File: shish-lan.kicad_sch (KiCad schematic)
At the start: 4 parts

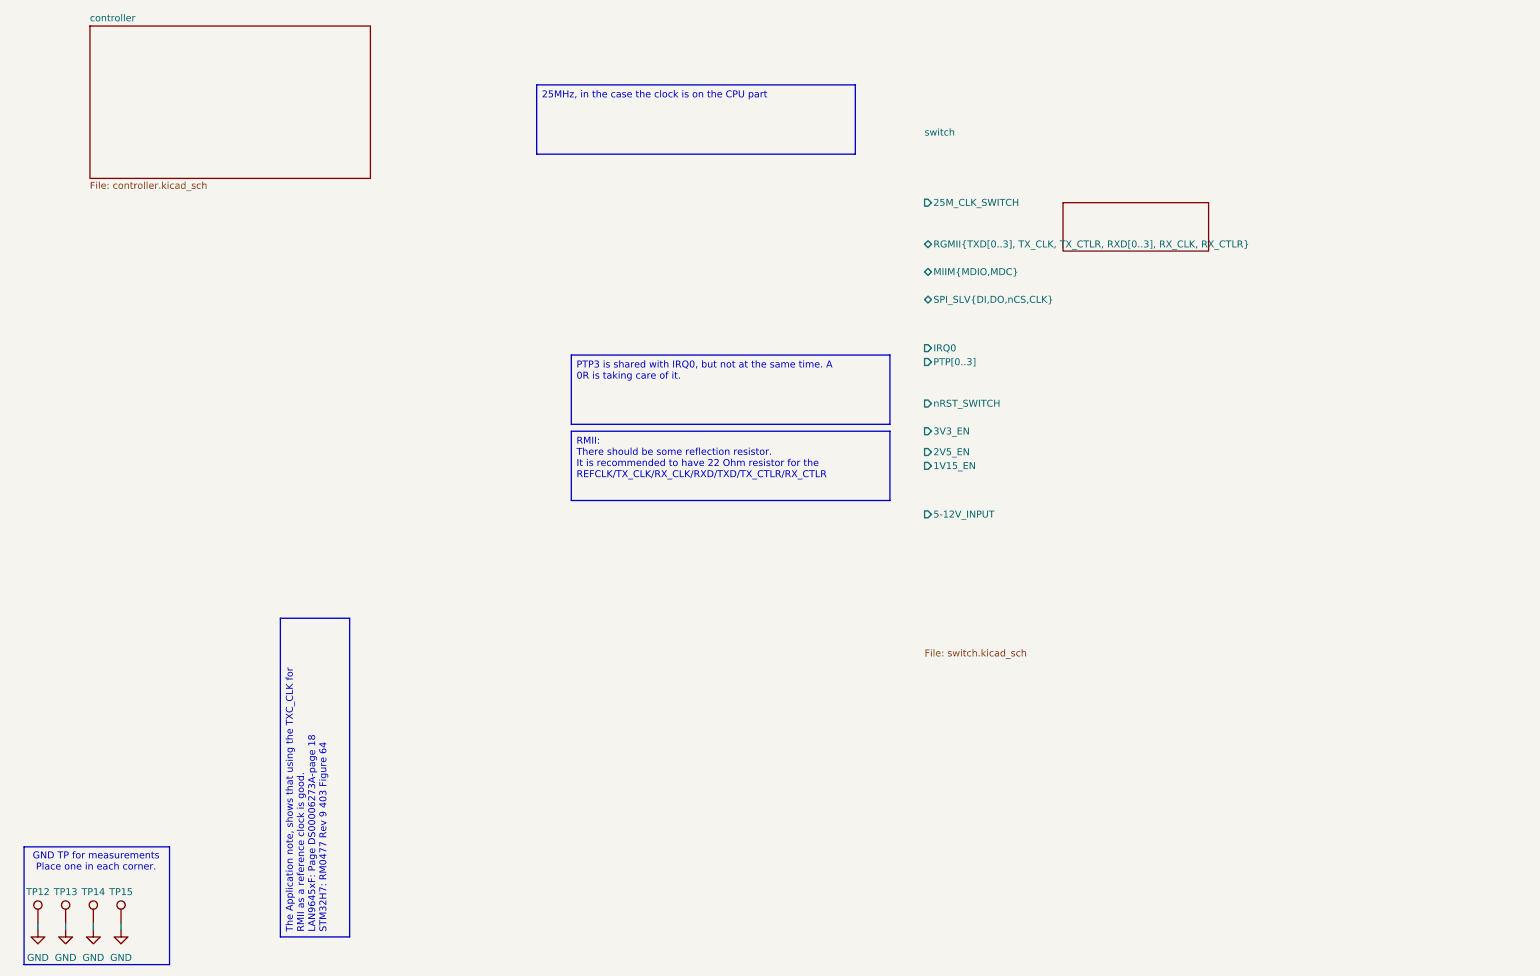
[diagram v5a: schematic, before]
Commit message: initial commit for GPIOs of STM32. Needs to resolve naming conflicts. Refs: #1
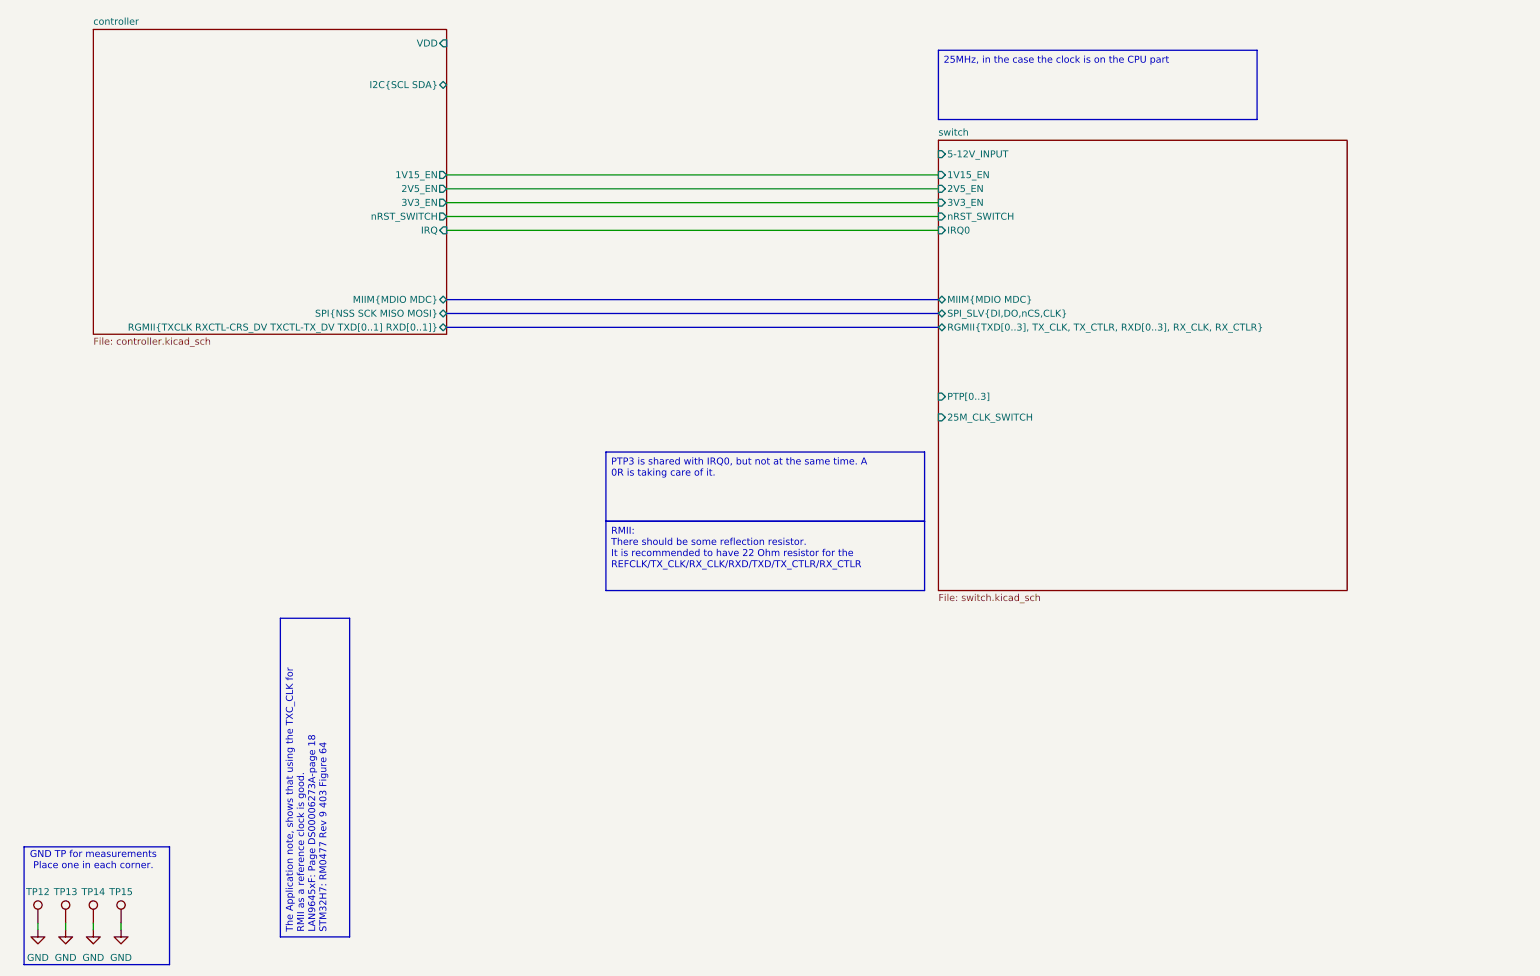
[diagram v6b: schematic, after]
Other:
- sheet controller ports: added 1V15_EN, 2V5_EN, 3V3_EN, I2C{SCL SDA}, IRQ, MIIM{MDIO MDC}, RGMII{TXCLK RXCTL-CRS_DV TXCTL-TX_DV TXD[0..1] RXD[0..1]}, SPI{NSS SCK MISO MOSI}, VDD, nRST_SWITCH; removed none
- sheet switch ports: added MIIM{MDIO MDC}; removed MIIM{MDIO,MDC}
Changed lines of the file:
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@@
 	(text "GND TP for measurements\nPlace one in each corner."
 		(exclude_from_sim no)
-		(at 30.988 176.784 0)
+		(at 30.48 176.53 0)
 		(effects
 			(font
@@
 	(text_box "RMII:\nThere should be some reflection resistor.\nIt is recommended to have 22 Ohm resistor for the REFCLK/TX_CLK/RX_CLK/RXD/TXD/TX_CTLR/RX_CTLR\n"
 		(exclude_from_sim no)
-		(at 118.11 97.79 0)
+		(at 124.46 114.3 0)
 		(size 58.42 12.7)
 		(margins 0.9525 0.9525 0.9525 0.9525)
@@
 	(text_box "25MHz, in the case the clock is on the CPU part"
 		(exclude_from_sim no)
-		(at 111.76 34.29 0)
+		(at 185.42 27.94 0)
 		(size 58.42 12.7)
 		(margins 0.9525 0.9525 0.9525 0.9525)
@@
 	(text_box "PTP3 is shared with IRQ0, but not at the same time. A 0R is taking care of it."
 		(exclude_from_sim no)
-		(at 118.11 83.82 0)
+		(at 124.46 101.6 0)
 		(size 58.42 12.7)
 		(margins 0.9525 0.9525 0.9525 0.9525)
@@
 	(wire
 		(pts
+			(xy 95.25 60.96) (xy 185.42 60.96)
+		)
+		(stroke
+			(width 0)
+			(type default)
+		)
+	)
+	(wire
+		(pts
 			(xy 25.4 189.23) (xy 25.4 187.96)
 		)
@@
 		)
 	)
+	(bus
+		(pts
+			(xy 95.25 76.2) (xy 185.42 76.2)
+		)
+		(stroke
+			(width 0)
+			(type default)
+		)
+	)
 	(wire
 		(pts
@@
 	(wire
 		(pts
+			(xy 95.25 50.8) (xy 185.42 50.8)
+		)
+		(stroke
+			(width 0)
+			(type default)
+		)
+	)
+	(bus
+		(pts
+			(xy 95.25 73.66) (xy 185.42 73.66)
+		)
+		(stroke
+			(width 0)
+			(type default)
+		)
+	)
+	(wire
+		(pts
+			(xy 95.25 55.88) (xy 185.42 55.88)
+		)
+		(stroke
+			(width 0)
+			(type default)
+		)
+	)
+	(wire
+		(pts
+			(xy 95.25 58.42) (xy 185.42 58.42)
+		)
+		(stroke
+			(width 0)
+			(type default)
+		)
+	)
+	(wire
+		(pts
+			(xy 95.25 53.34) (xy 185.42 53.34)
+		)
+		(stroke
+			(width 0)
+			(type default)
+		)
+	)
+	(bus
+		(pts
+			(xy 95.25 78.74) (xy 185.42 78.74)
+		)
+		(stroke
+			(width 0)
+			(type default)
+		)
+	)
+	(wire
+		(pts
 			(xy 30.48 189.23) (xy 30.48 187.96)
 		)
@@
 	)
 	(sheet
-		(at 29.845 23.495)
-		(size 51.435 27.94)
+		(at 30.48 24.13)
+		(size 64.77 55.88)
 		(exclude_from_sim no)
 		(in_bom yes)
@@
 		)
 		(property "Sheetname" "controller"
-			(at 29.845 22.7834 0)
+			(at 30.48 23.4184 0)
 			(effects
 				(font
@@
 		)
 		(property "Sheetfile" "controller.kicad_sch"
-			(at 29.845 52.0196 0)
+			(at 30.48 80.5946 0)
 			(effects
 				(font
@@
 			)
 		)
+		(pin "I2C{SCL SDA}" bidirectional
+			(at 95.25 34.29 0)
+			(effects
+				(font
+					(size 1.27 1.27)
+				)
+				(justify right)
+			)
+		)
+		(pin "MIIM{MDIO MDC}" bidirectional
+			(at 95.25 73.66 0)
+			(effects
+				(font
+					(size 1.27 1.27)
+				)
+				(justify right)
+			)
+		)
+		(pin "RGMII{TXCLK RXCTL-CRS_DV TXCTL-TX_DV TXD[0..1] RXD[0..1]}" bidirectional
+			(at 95.25 78.74 0)
+			(effects
+				(font
+					(size 1.27 1.27)
+				)
+				(justify right)
+			)
+		)
+		(pin "SPI{NSS SCK MISO MOSI}" bidirectional
+			(at 95.25 76.2 0)
+			(effects
+				(font
+					(size 1.27 1.27)
+				)
+				(justify right)
+			)
+		)
+		(pin "VDD" input
+			(at 95.25 26.67 0)
+			(effects
+				(font
+					(size 1.27 1.27)
+				)
+				(justify right)
+			)
+		)
+		(pin "1V15_EN" output
+			(at 95.25 50.8 0)
+			(effects
+				(font
+					(size 1.27 1.27)
+				)
+				(justify right)
+			)
+		)
+		(pin "2V5_EN" output
+			(at 95.25 53.34 0)
+			(effects
+				(font
+					(size 1.27 1.27)
+				)
+				(justify right)
+			)
+		)
+		(pin "3V3_EN" output
+			(at 95.25 55.88 0)
+			(effects
+				(font
+					(size 1.27 1.27)
+				)
+				(justify right)
+			)
+		)
+		(pin "nRST_SWITCH" output
+			(at 95.25 58.42 0)
+			(effects
+				(font
+					(size 1.27 1.27)
+				)
+				(justify right)
+			)
+		)
+		(pin "IRQ" input
+			(at 95.25 60.96 0)
+			(effects
+				(font
+					(size 1.27 1.27)
+				)
+				(justify right)
+			)
+		)
 		(instances
 			(project "shish-lan"
@@
 	)
 	(sheet
-		(at 208.28 55.88)
-		(size 26.67 8.89)
+		(at 185.42 44.45)
+		(size 74.93 82.55)
 		(exclude_from_sim no)
 		(in_bom yes)
@@
 		)
 		(property "Sheetname" "switch"
-			(at 182.88 43.7384 0)
+			(at 185.42 43.7384 0)
 			(effects
 				(font
@@
 		)
 		(property "Sheetfile" "switch.kicad_sch"
-			(at 182.88 137.7446 0)
+			(at 185.42 127.5846 0)
 			(effects
 				(font
@@
 			)
 		)
-		(pin "5-12V_INPUT" input
-			(at 182.88 113.03 180)
+		(pin "1V15_EN" input
+			(at 185.42 50.8 180)
 			(effects
 				(font
@@
 			)
 		)
-		(pin "RGMII{TXD[0..3], TX_CLK, TX_CTLR, RXD[0..3], RX_CLK, RX_CTLR}" bidirectional
-			(at 182.88 63.5 180)
+		(pin "2V5_EN" input
+			(at 185.42 53.34 180)
 			(effects
 				(font
@@
 			)
 		)
-		(pin "MIIM{MDIO,MDC}" bidirectional
-			(at 182.88 68.58 180)
+		(pin "3V3_EN" input
+			(at 185.42 55.88 180)
 			(effects
 				(font
@@
 			)
 		)
-		(pin "nRST_SWITCH" input
-			(at 182.88 92.71 180)
+		(pin "5-12V_INPUT" input
+			(at 185.42 46.99 180)
 			(effects
 				(font
@@
 			)
 		)
-		(pin "PTP[0..3]" input
-			(at 182.88 85.09 180)
+		(pin "25M_CLK_SWITCH" input
+			(at 185.42 95.25 180)
 			(effects
 				(font
@@
 			)
 		)
-		(pin "SPI_SLV{DI,DO,nCS,CLK}" bidirectional
-			(at 182.88 73.66 180)
+		(pin "IRQ0" input
+			(at 185.42 60.96 180)
 			(effects
 				(font
@@
 			)
 		)
-		(pin "25M_CLK_SWITCH" input
-			(at 182.88 55.88 180)
+		(pin "MIIM{MDIO MDC}" bidirectional
+			(at 185.42 73.66 180)
 			(effects
 				(font
@@
 			)
 		)
-		(pin "2V5_EN" input
-			(at 182.88 101.6 180)
+		(pin "nRST_SWITCH" input
+			(at 185.42 58.42 180)
 			(effects
 				(font
@@
 			)
 		)
-		(pin "3V3_EN" input
-			(at 182.88 97.79 180)
+		(pin "PTP[0..3]" input
+			(at 185.42 91.44 180)
 			(effects
 				(font
@@
 			)
 		)
-		(pin "1V15_EN" input
-			(at 182.88 104.14 180)
+		(pin "RGMII{TXD[0..3], TX_CLK, TX_CTLR, RXD[0..3], RX_CLK, RX_CTLR}" bidirectional
+			(at 185.42 78.74 180)
 			(effects
 				(font
@@
 			)
 		)
-		(pin "IRQ0" input
-			(at 182.88 82.55 180)
+		(pin "SPI_SLV{DI,DO,nCS,CLK}" bidirectional
+			(at 185.42 76.2 180)
 			(effects
 				(font

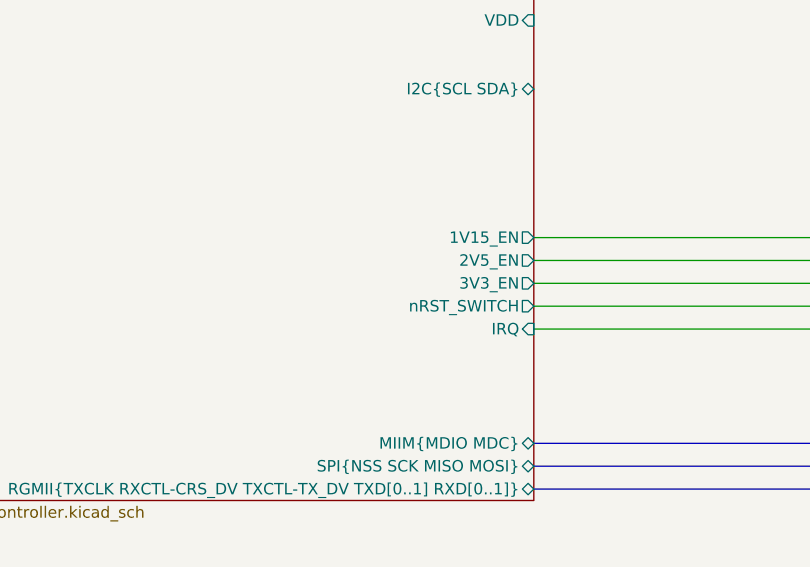
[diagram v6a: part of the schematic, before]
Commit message: updates buck enable, rst and IRQ to new naming scheme. Refs: #1
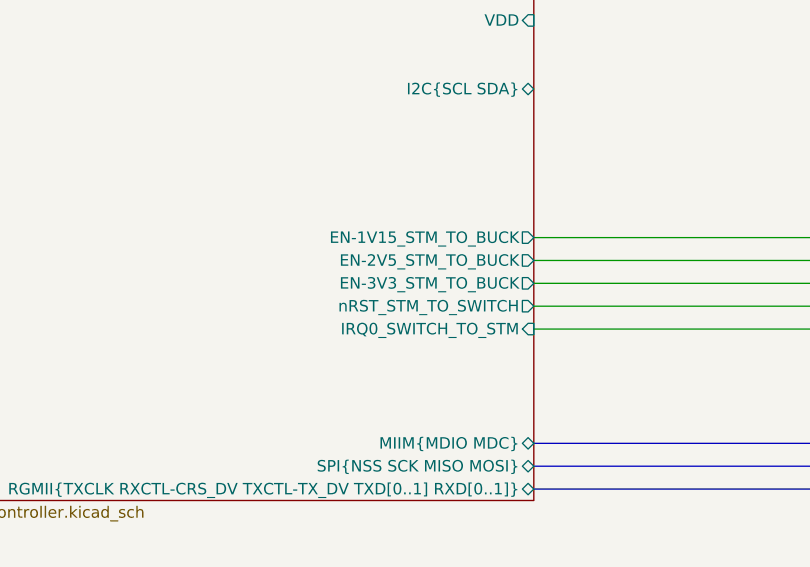
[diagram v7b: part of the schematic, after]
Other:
- sheet controller ports: added EN-1V15_STM_TO_BUCK, EN-2V5_STM_TO_BUCK, EN-3V3_STM_TO_BUCK, IRQ0_SWITCH_TO_STM, nRST_STM_TO_SWITCH; removed 1V15_EN, 2V5_EN, 3V3_EN, IRQ, nRST_SWITCH
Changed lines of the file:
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@@
 			)
 		)
-		(pin "1V15_EN" output
+		(pin "EN-1V15_STM_TO_BUCK" output
 			(at 95.25 50.8 0)
 			(effects
@@
 			)
 		)
-		(pin "2V5_EN" output
+		(pin "EN-2V5_STM_TO_BUCK" output
 			(at 95.25 53.34 0)
 			(effects
@@
 			)
 		)
-		(pin "3V3_EN" output
+		(pin "EN-3V3_STM_TO_BUCK" output
 			(at 95.25 55.88 0)
 			(effects
@@
 			)
 		)
-		(pin "nRST_SWITCH" output
+		(pin "nRST_STM_TO_SWITCH" output
 			(at 95.25 58.42 0)
 			(effects
@@
 			)
 		)
-		(pin "IRQ" input
+		(pin "IRQ0_SWITCH_TO_STM" input
 			(at 95.25 60.96 0)
 			(effects

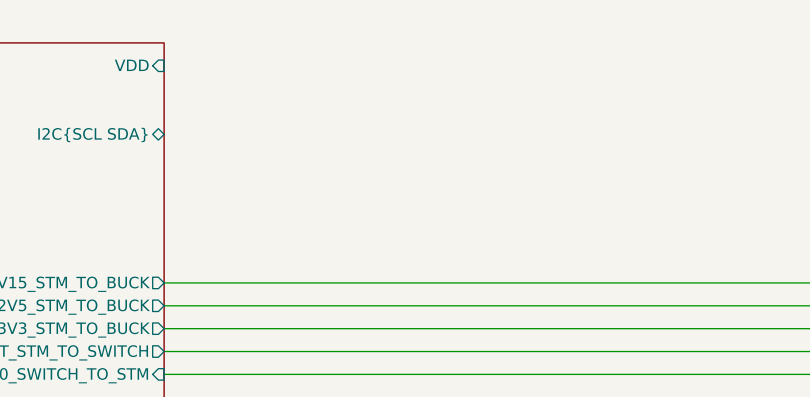
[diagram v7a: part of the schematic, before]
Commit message: adds I2C Pull up and test points. Refs: #1
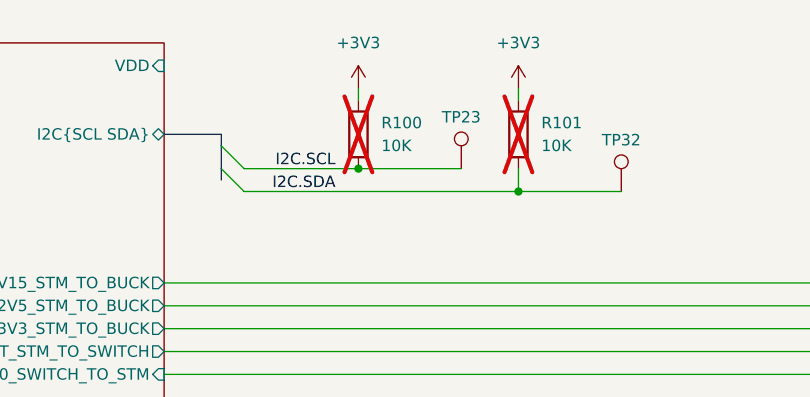
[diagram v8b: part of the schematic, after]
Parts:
- added R100, R101: 10K, KL_Footprints:C_0603, symbol KL_R:R_10K_100mW_5_0603
- added TP23, TP32: ~, Connector_PinHeader_2.54mm:PinHeader_1x01_P2.54mm_Vertical, symbol KL_TP:TestPoint
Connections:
- new net +3V3: R100.1, R101.1
- new net I2C.SCL: R100.2, TP23.1
- new net I2C.SDA: R101.2, TP32.1
